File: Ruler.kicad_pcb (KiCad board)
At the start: 2 copper layers, 162.1 x 30 mm, 54 parts, among them J1 USB_C_Receptacle_USB2.0

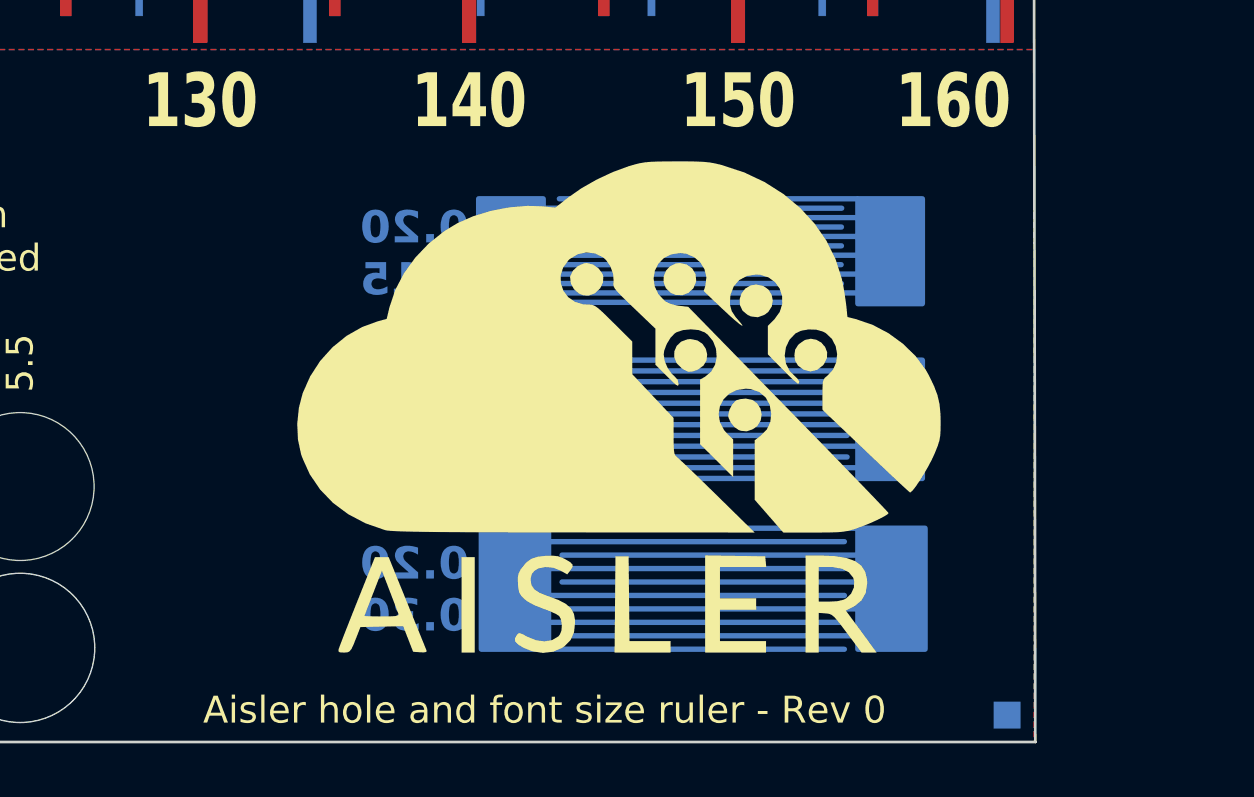
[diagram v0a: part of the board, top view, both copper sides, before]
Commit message: Added vias and transparency
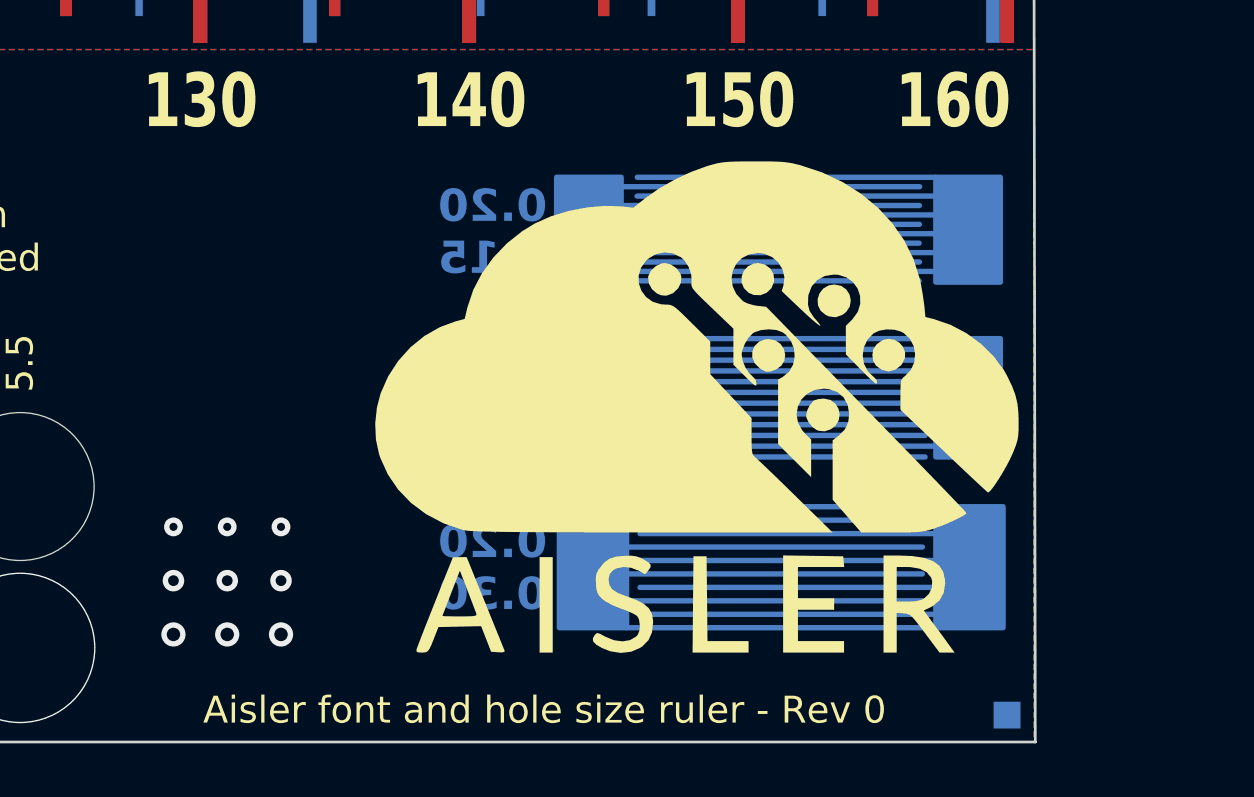
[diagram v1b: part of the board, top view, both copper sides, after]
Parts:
- moved G*** 2.90 mm to (169.9, 85.2)
- moved G*** 2.90 mm to (169.0, 94.9)
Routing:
- net (no net): vias 0 -> 9
- added copper zone on B.Cu, net (none)
- added copper zone on F.Cu, net (none)
- removed copper zone on B.Cu, net GND
- removed copper zone on F.Cu, net GND
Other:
- board text added: "0.3 0.4 0.5"
- board text added: "Aisler font and hole size ruler - Rev 0"
- board text removed: "Aisler hole and font size ruler - Rev 0"

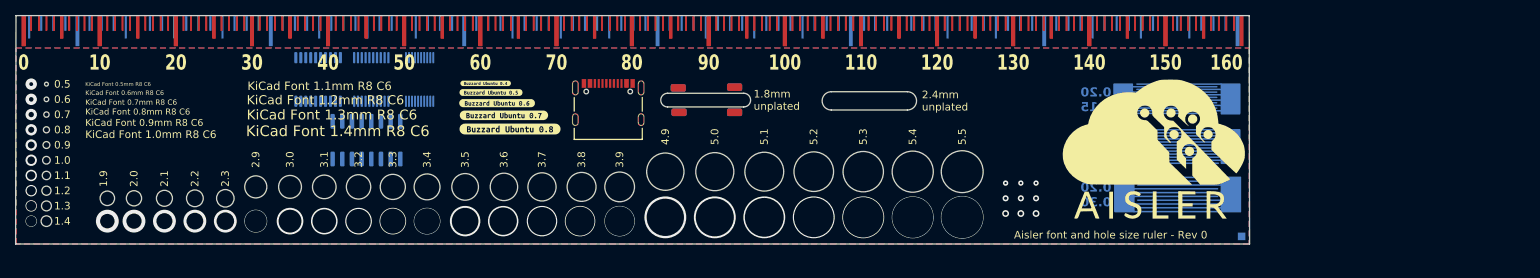
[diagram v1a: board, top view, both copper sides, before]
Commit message: Fix soldermask pullback on vias
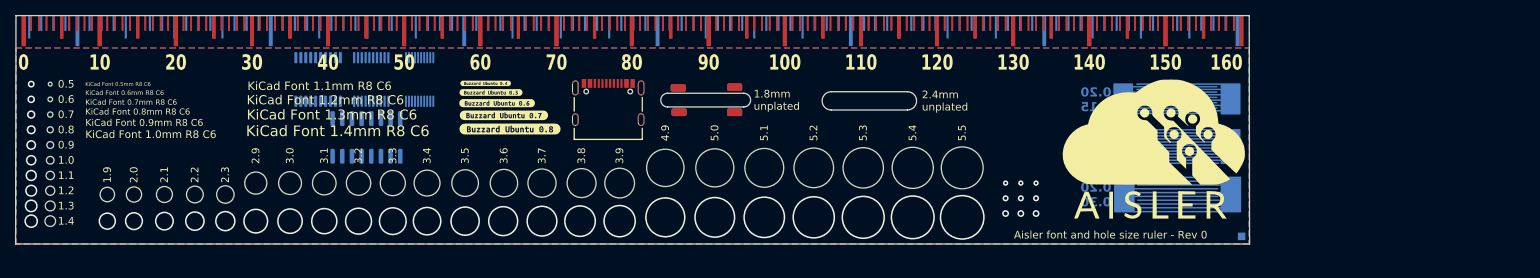
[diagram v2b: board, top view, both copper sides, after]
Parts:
- moved REF** 0.50 mm to (24.5, 97.0)
- moved REF** 0.50 mm to (94.3, 92.0)
- moved REF** 0.50 mm to (131.3, 90.0)
- moved REF** 0.50 mm to (89.1, 92.0)
- moved REF** 0.50 mm to (24.5, 83.0)
- moved REF** 0.50 mm to (79.0, 92.0)
- moved REF** 0.50 mm to (56.0, 92.0)
- moved REF** 0.50 mm to (84.1, 92.0)
- moved REF** 0.50 mm to (24.5, 89.0)
- moved REF** 0.50 mm to (144.3, 90.0)
- moved REF** 0.50 mm to (74.0, 92.0)
- moved REF** 0.50 mm to (24.5, 81.0)
- moved REF** 0.50 mm to (24.5, 87.0)
- moved REF** 0.50 mm to (65.0, 92.0)
- moved REF** 0.50 mm to (60.5, 92.0)
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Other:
- board text added: "0.15"
- board text added: "0.20"
- board text removed: "0.15mm"
- board text removed: "0.20mm"

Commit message: Add custome bridges
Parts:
- moved ? 30.0 mm to (144.4, 79.4) (x2)
- moved ? 30.0 mm to (137.1, 82.7) (x2)
- moved ? 30.0 mm to (137.0, 79.5) (x2)
- moved ? 30.0 mm to (144.4, 82.7) (x2)
- moved J1 30.0 mm to (127.8, 81.4)
- moved REF** 30.0 mm to (54.5, 97.0)
- moved REF** 30.0 mm to (124.3, 92.0)
- moved REF** 30.0 mm to (161.3, 90.0)
- moved REF** 30.0 mm to (119.1, 92.0)
- moved REF** 30.0 mm to (54.5, 83.0)
- moved REF** 30.0 mm to (109.0, 92.0)
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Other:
- board size 162.1 x 30 mm -> 166.8 x 32.4 mm

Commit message: Update for Twitter giveaway
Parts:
- removed G*** (x2): LOGO, LOGO
- added ?: , , B.Cu at (160.0, 79.7)
- added ?: , , B.Cu at (167.4, 82.6)
- added ?: , , B.Cu at (160.1, 82.6)
- added ?: , , B.Cu at (167.4, 79.7)
- added ?: , , F.Cu at (167.4, 79.7)
- added ?: , , F.Cu at (167.4, 82.6)
- added ?: , , F.Cu at (160.0, 79.7)
- added ?: , , F.Cu at (160.1, 82.6)
- REF**: moved to B.Cu
- moved ? 3.01 mm to (147.4, 79.7) (x2)
- moved ? 3.01 mm to (140.1, 82.5) (x2)
- moved ? 3.01 mm to (140.0, 79.7) (x2)
- moved ? 3.01 mm to (147.4, 82.5) (x2)
- turned REF** to 180 degrees
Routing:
- removed copper zone on B.Cu, net (none)
- removed copper zone on F.Cu, net (none)
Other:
- board size 166.8 x 32.4 mm -> 162 x 30 mm
- board text added: "0.10"
- board text added: "0.25"
- board text added: "0.30"
- board text added: "0.35"
- board text added: "0.40"
- board text added: "0.45"
- board text added: "0.50"
- board text added: "0.55"
- board text added: "0.60"
- board text added: "1.6mm unplated"
- board text added: "1.7mm unplated"
- board text added: "@matseng"
- board text added: "Font and hole size ruler - Rev 1"
- board text removed: "1.8mm unplated"
- board text removed: "2.4mm unplated"
- board text removed: "Aisler font and hole size ruler - Rev 0"
